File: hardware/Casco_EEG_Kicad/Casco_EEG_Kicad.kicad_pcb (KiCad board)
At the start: 2 copper layers, 123 x 64.5 mm, 117 parts, among them J1 Jack_Touch-Proof, J10 Jack_Touch-Proof, J11 FTSH-105-XX-X-DV, J13 Conn_01x09_Pin, J15 USB4125-GF-A_REVA2, J2 Jack_Touch-Proof, J3 Jack_Touch-Proof, J4 Jack_Touch-Proof, J5 Jack_Touch-Proof, J6 Jack_Touch-Proof, J7 Jack_Touch-Proof, J8 Jack_Touch-Proof, J9 Jack_Touch-Proof, Q1 FS8205A, SW1 SW_Push, SW2 PCM12SMTR, U1 ADS1299, U2 HC-05, U3 LPC845M301JBD48E, U4 TP4056-42-ESOP8, U5 DW01A, U7 AP2112K-3.3TRG1

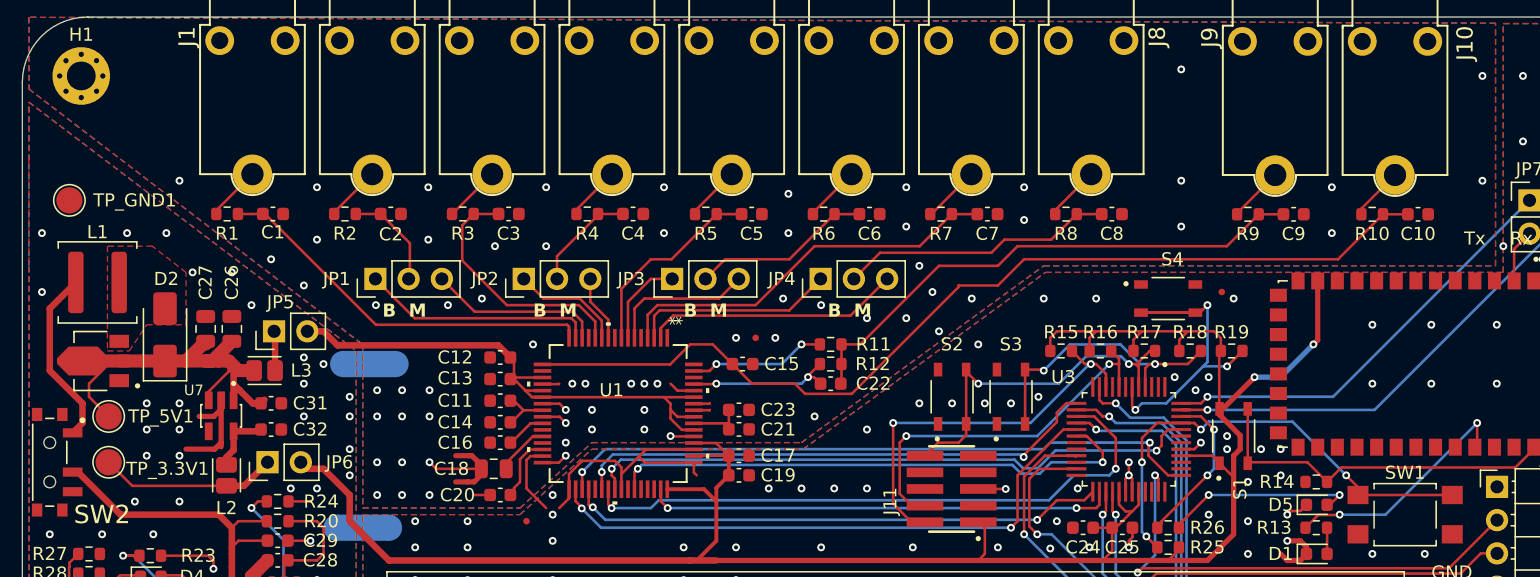
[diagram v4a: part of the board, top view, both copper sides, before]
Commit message: Agrego protecciones a las entradas analogicas, quito jumpers dealimentacion, agrego capacitores al HC05
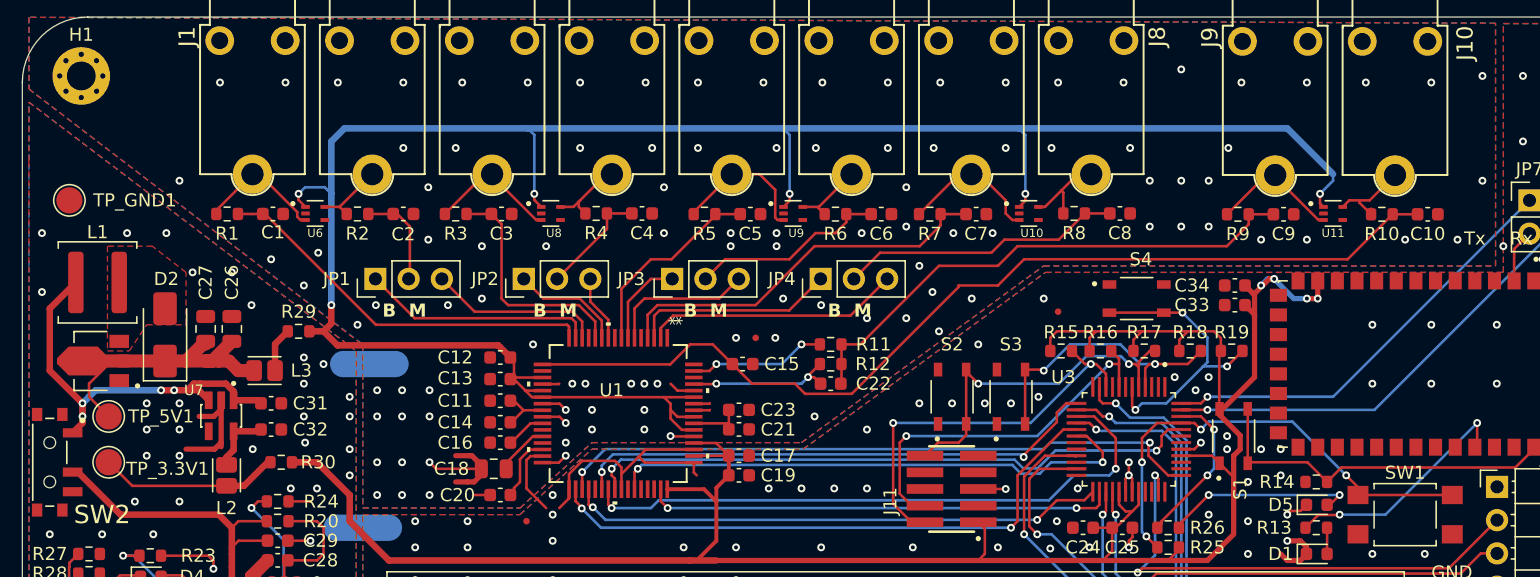
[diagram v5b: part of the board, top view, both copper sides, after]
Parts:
- removed JP5, JP6: Jumper_2_Open, Connector_PinHeader_2.54mm:PinHeader_1x02_P2.54mm_Vertical
- added C33: 10u, Capacitor_SMD:C_0603_1608Metric, F.Cu at (176.5, 87.0)
- added C34: 0.1u, Capacitor_SMD:C_0603_1608Metric, F.Cu at (176.5, 85.5)
- added R29: 0, Resistor_SMD:R_0603_1608Metric, F.Cu at (105.0, 89.0)
- added R30: 0, Resistor_SMD:R_0603_1608Metric, F.Cu at (103.7, 99.0)
- added U10: TPD2E001DRLR, Huellas:SOT50P160X60-5N, F.Cu at (160.8, 80.0)
- added U11: TPD2E001DRLR, Huellas:SOT50P160X60-5N, F.Cu at (184.0, 80.0)
- added U6: TPD2E001DRLR, Huellas:SOT50P160X60-5N, F.Cu at (106.3, 80.0)
- added U8: TPD2E001DRLR, Huellas:SOT50P160X60-5N, F.Cu at (124.3, 80.0)
- added U9: TPD2E001DRLR, Huellas:SOT50P160X60-5N, F.Cu at (142.8, 80.0)
- moved FID3 12.6 mm to (163.0, 87.5)
- moved S4 2.41 mm to (169.0, 86.5)
- moved C2 0.95 mm to (113.0, 80.0)
- moved R2 0.95 mm to (109.5, 80.0)
- moved C6 0.90 mm to (149.5, 80.1)
- moved R6 0.90 mm to (146.0, 80.1)
- moved C7 0.86 mm to (156.7, 80.1)
- moved R7 0.86 mm to (153.2, 80.1)
- moved C9 0.77 mm to (180.2, 80.1)
- moved R9 0.77 mm to (176.7, 80.1)
- moved C10 0.74 mm to (191.2, 80.1)
- moved R10 0.74 mm to (187.7, 80.1)
- moved C4 0.68 mm to (131.2, 80.0)
- moved R4 0.68 mm to (127.7, 80.0)
- moved C8 0.62 mm to (167.7, 80.0)
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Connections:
- C26 pad 1: /Alimentacion/5V_reg -> Net-(D2-K)
- C27 pad 1: /Alimentacion/5V_reg -> Net-(D2-K)
- C31 pad 1: /Alimentacion/5V_reg -> /Alimentacion/VBATP
- D2 pad 1: /Alimentacion/5V_reg -> Net-(D2-K)
- L1 pad 1: Net-(L1-Pad1) -> /Alimentacion/VBATP
- L3 pad 1: /Alimentacion/5V_reg -> Net-(D2-K)
- PS1 pad 2: /Alimentacion/5V_reg -> Net-(D2-K)
- SW2 pad 1: Net-(L1-Pad1) -> /Alimentacion/VBATP
- TP_5V1 pad 1: /Alimentacion/5V_reg -> Net-(D2-K)
- U7 pad 1: /Alimentacion/5V_reg -> /Alimentacion/VBATP
- U7 pad 3: /Alimentacion/5V_reg -> /Alimentacion/VBATP
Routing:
- net +5V: track 41.9 -> 161.2 mm, vias 0 -> 6
- net /Alimentacion/VBATP: track 0.00 -> 33.6 mm, vias 0 -> 4
- net /Alimentacion/5V_reg: track 32.5 -> 0.00 mm
- net Net-(D2-K): track 0.00 -> 23.5 mm
- net Net-(L1-Pad1): track 15.4 -> 0.00 mm
- net +3.3V: track 165.8 -> 173.9 mm, vias 2 -> 4
- net Net-(U9-IO1): track 4.21 -> 10.9 mm
- net Net-(U10-IO1): track 4.41 -> 11.0 mm
- net Net-(U11-IO1): track 4.43 -> 10.4 mm
- net Net-(U8-IO1): track 4.32 -> 10.2 mm
- net Net-(U6-IO1): track 4.18 -> 9.89 mm
- net /CPU/PIO0_04: track 26.2 -> 22.5 mm
- net Net-(U11-IO2): track 4.06 -> 6.87 mm
- net Net-(U10-IO2): track 4.19 -> 6.88 mm
- net Net-(U8-IO2): track 4.16 -> 6.21 mm
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
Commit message: Cambio jumpers
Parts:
- removed R29, R30: 0, Resistor_SMD:R_0603_1608Metric
- added JP5: Jumper_2_Open, Jumper:SolderJumper-2_P1.3mm_Open_RoundedPad1.0x1.5mm, F.Cu at (104.2, 89.0)
- added JP6: Jumper_2_Open, Jumper:SolderJumper-2_P1.3mm_Open_RoundedPad1.0x1.5mm, F.Cu at (103.3, 99.0)
- moved R4 0.78 mm to (128.5, 80.0)
- moved R2 0.50 mm to (110.0, 80.0)
- moved R6 0.50 mm to (146.5, 80.1)
- moved U8 0.47 mm to (124.7, 80.0)
- moved C4 0.28 mm to (131.5, 80.0)
- moved R8 0.28 mm to (164.5, 80.0)
- moved C9 0.22 mm to (180.0, 80.1)
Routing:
- net GNDA: track 24.4 -> 32.2 mm
- net GNDD: track 42.1 -> 45.5 mm, vias 86 -> 95
- net +3.3V: track 173.9 -> 175.3 mm
- net +5V: track 161.2 -> 162.4 mm
- net Net-(U9-IO2): track 5.60 -> 6.54 mm
- net Net-(U8-IO1): track 10.2 -> 11.1 mm

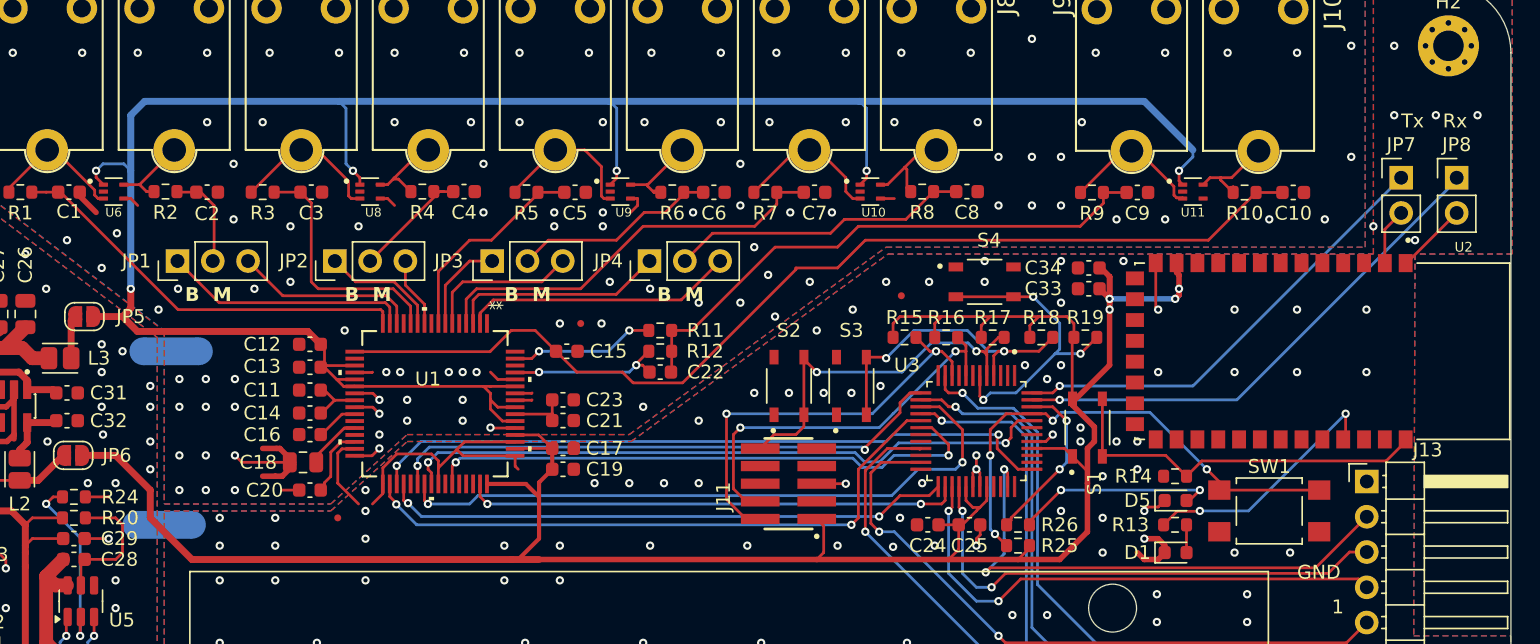
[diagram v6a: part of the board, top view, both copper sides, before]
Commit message: Agrego GND para puente UART al modulo BT
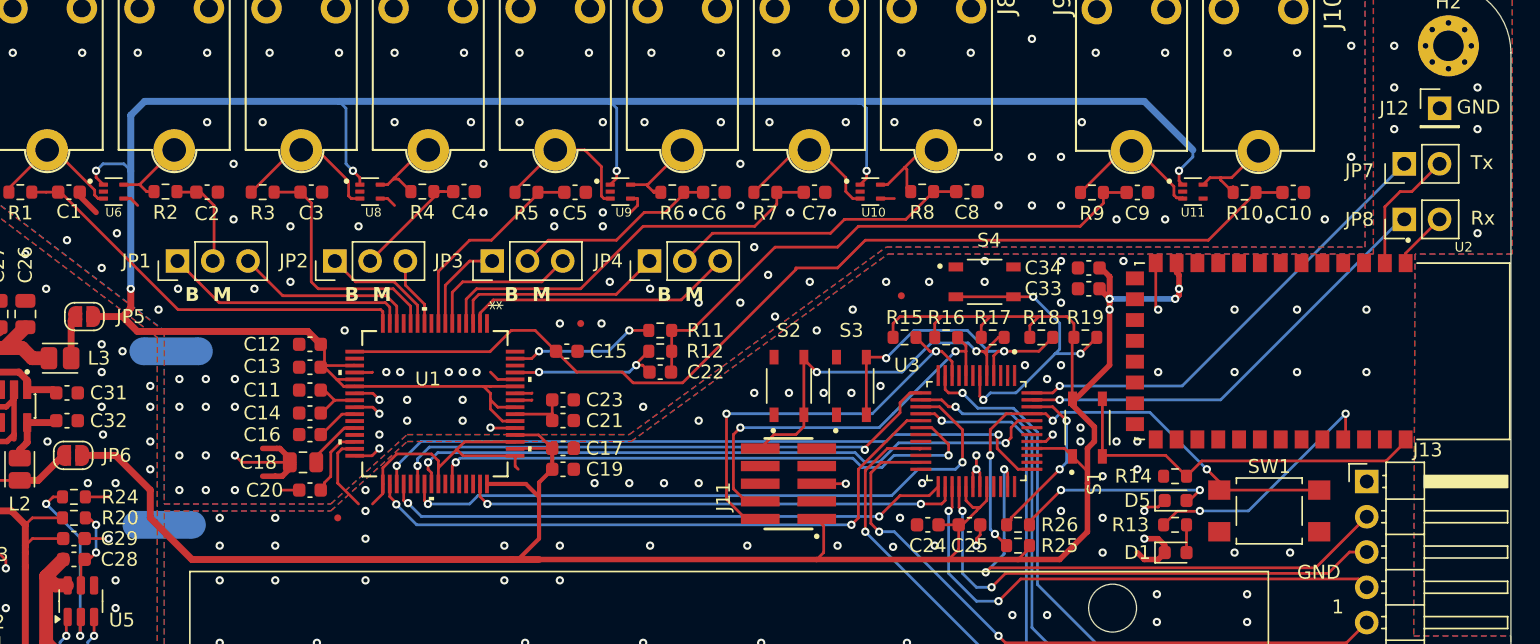
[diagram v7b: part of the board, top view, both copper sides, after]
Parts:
- added J12: Conn_01x01_Pin, Connector_PinHeader_2.54mm:PinHeader_1x01_P2.54mm_Vertical, F.Cu at (201.8, 74.0)
- moved JP8 4.82 mm to (199.2, 82.0), turned to 90 degrees
- moved JP7 1.02 mm to (199.2, 78.0), turned to 90 degrees
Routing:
- net Net-(JP7-B): track 4.10 -> 9.28 mm
- net /CPU/RX_Master: track 37.8 -> 32.7 mm
- net Net-(U5-VCC): track 9.80 -> 5.99 mm, vias 0 -> 2
- net Net-(JP8-B): track 5.17 -> 4.23 mm

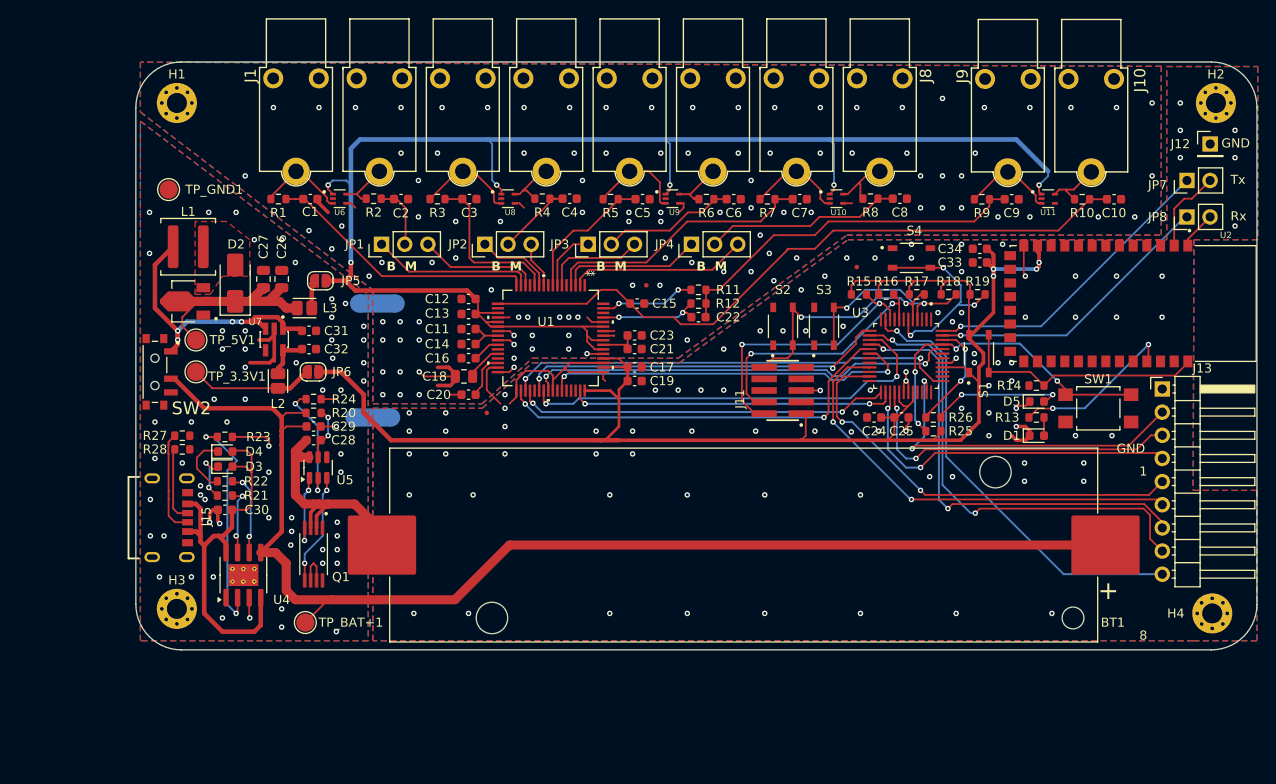
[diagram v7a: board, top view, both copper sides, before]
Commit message: Actualización de pcb con aislamiento dc/dc, elimino entradas de trigger
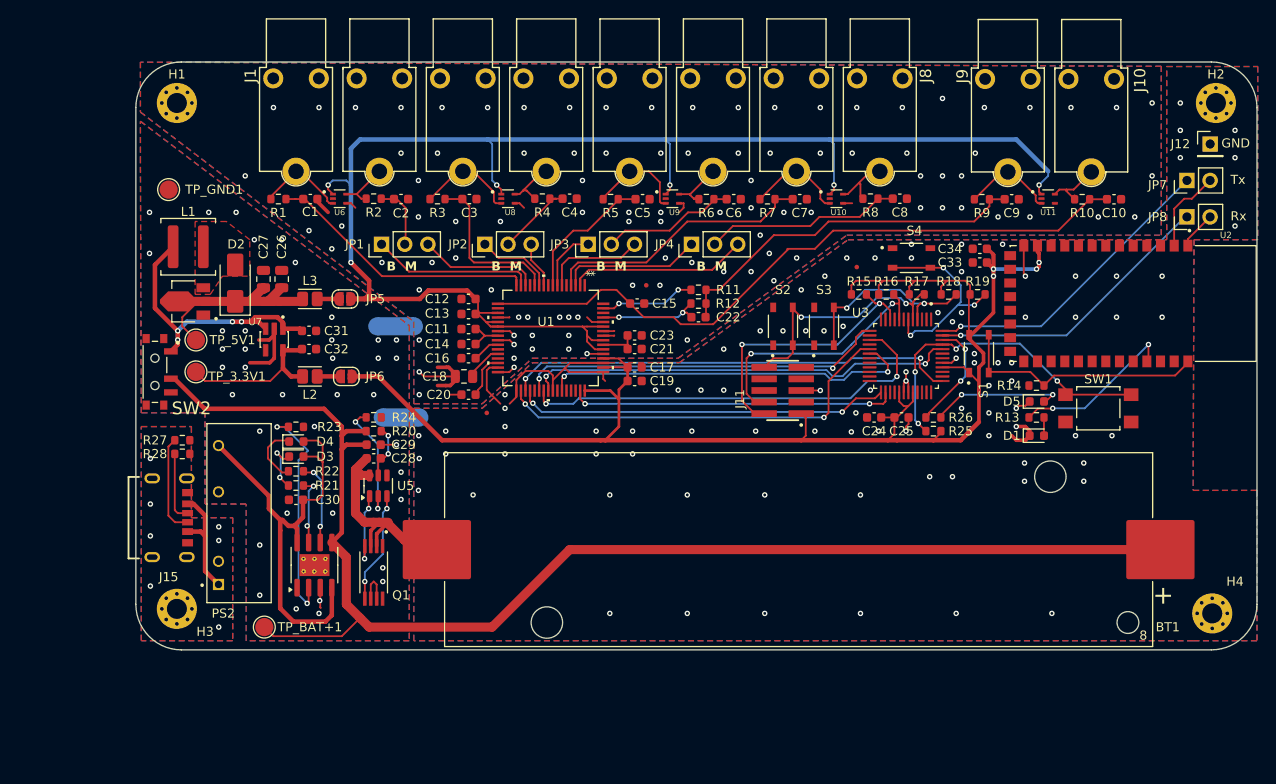
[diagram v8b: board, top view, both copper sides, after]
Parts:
- removed J13: Conn_01x09_Pin, Connector_PinHeader_2.54mm:PinHeader_1x09_P2.54mm_Horizontal
- added PS2: RP-0505S, Huellas:CONV_RP-0505S, F.Cu at (93.0, 114.7)
- moved C30 7.87 mm to (101.5, 113.0)
- moved D3 7.87 mm to (101.5, 108.3)
- moved D4 7.87 mm to (101.5, 106.6)
- moved R21 7.87 mm to (101.5, 111.5)
- moved R22 7.87 mm to (101.5, 109.9)
- moved R23 7.87 mm to (101.5, 105.0)
- moved U4 7.87 mm to (103.5, 120.2)
- moved C28 6.89 mm to (110.0, 108.5)
- moved C29 6.89 mm to (110.0, 107.0)
- moved Q1 6.89 mm to (110.0, 121.0)
- moved R20 6.89 mm to (110.0, 105.5)
- moved R24 6.89 mm to (110.0, 104.0)
- moved U5 6.89 mm to (110.5, 111.5)
- moved BT1 6.05 mm to (156.6, 118.5)
- moved TP_BAT+1 4.53 mm to (98.0, 127.0)
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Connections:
- J15 pad A12: GNDPWR -> GNDPWR_NOAISL
- J15 pad A9: /Alimentacion/V_BUSP -> /Alimentacion/V_BUSP_NOAISL
- J15 pad B12: GNDPWR -> GNDPWR_NOAISL
- J15 pad B9: /Alimentacion/V_BUSP -> /Alimentacion/V_BUSP_NOAISL
- J15 pad S1: GNDPWR -> GNDPWR_NOAISL
- J15 pad S2: GNDPWR -> GNDPWR_NOAISL
- J15 pad S3: GNDPWR -> GNDPWR_NOAISL
- J15 pad S4: GNDPWR -> GNDPWR_NOAISL
- R27 pad 2: GNDPWR -> GNDPWR_NOAISL
- R28 pad 2: GNDPWR -> GNDPWR_NOAISL
- TP_3.3V1 pad 1: Net-(JP6-A) -> Net-(U7-VOUT)
- U3 pad 11: Net-(J13-Pin_9) -> unconnected-(U3-PIO1_0/CAPT_X1-Pad11)
- U3 pad 14: Net-(J13-Pin_8) -> unconnected-(U3-PIO1_1/CAPT_X2-Pad14)
- U3 pad 16: Net-(J13-Pin_7) -> unconnected-(U3-PIO1_2/CAPT_X3_-Pad16)
- U3 pad 21: Net-(J13-Pin_6) -> unconnected-(U3-PIO1_3/CAPT_X4-Pad21)
- U3 pad 23: Net-(J13-Pin_5) -> unconnected-(U3-PIO1_4/CAPT_X5-Pad23)
- U3 pad 27: Net-(J13-Pin_4) -> unconnected-(U3-PIO1_5/CAPT_X6-Pad27)
- U3 pad 28: Net-(J13-Pin_3) -> unconnected-(U3-PIO1_6/CAPT_X7-Pad28)
- U3 pad 35: Net-(J13-Pin_2) -> unconnected-(U3-PIO1_7/CAPT_X8-Pad35)
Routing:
- net Net-(J13-Pin_8): track 52.0 -> 0.00 mm, vias 2 -> 0
- net Net-(J13-Pin_7): track 50.2 -> 0.00 mm, vias 2 -> 0
- net Net-(J13-Pin_6): track 49.3 -> 0.00 mm, vias 2 -> 0
- net Net-(J13-Pin_9): track 49.0 -> 0.00 mm, vias 1 -> 0
- net Net-(J13-Pin_5): track 47.5 -> 0.00 mm, vias 2 -> 0
- net Net-(J13-Pin_2): track 38.4 -> 0.00 mm, vias 2 -> 0
- net Net-(J13-Pin_4): track 38.2 -> 0.00 mm, vias 2 -> 0
- net Net-(J13-Pin_3): track 36.9 -> 0.00 mm, vias 2 -> 0
- net /Alimentacion/V_BUSP_NOAISL: track 0.00 -> 12.7 mm
- net Net-(U7-VOUT): track 5.56 -> 17.2 mm
- net /Alimentacion/VOUT+: track 141.4 -> 153.0 mm
- net Net-(JP6-A): track 13.6 -> 2.55 mm
- net GNDPWR: track 27.1 -> 16.7 mm, vias 63 -> 38
- net /Alimentacion/V_BAT_N: track 29.7 -> 23.1 mm
- net +3.3V: track 175.3 -> 170.3 mm
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- added copper zone on B.Cu, net GNDPWR_NOAISL
- added copper zone on F.Cu, net GNDPWR_NOAISL
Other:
- board text removed: "1"
